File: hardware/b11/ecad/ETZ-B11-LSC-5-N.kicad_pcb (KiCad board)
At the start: 2 copper layers, 112.3 x 85.8 mm, 36 parts, among them SW1 MX-Hotswap-1U, SW10 MX-Hotswap-1U, SW11 MX-Hotswap-1U, SW12 MX-Hotswap-1U, SW13 MX-Hotswap-1U, SW14 MX-Hotswap-1U, SW15 MX-Hotswap-1U, SW16 MX-Hotswap-1U, SW17 MX-Hotswap-1U, SW18 MX-Hotswap-1U, SW2 MX-Hotswap-1U, SW3 MX-Hotswap-1U, SW4 MX-Hotswap-1U, SW5 MX-Hotswap-1U, SW6 MX-Hotswap-1U, SW7 MX-Hotswap-1U, SW8 MX-Hotswap-1U, SW9 MX-Hotswap-1U

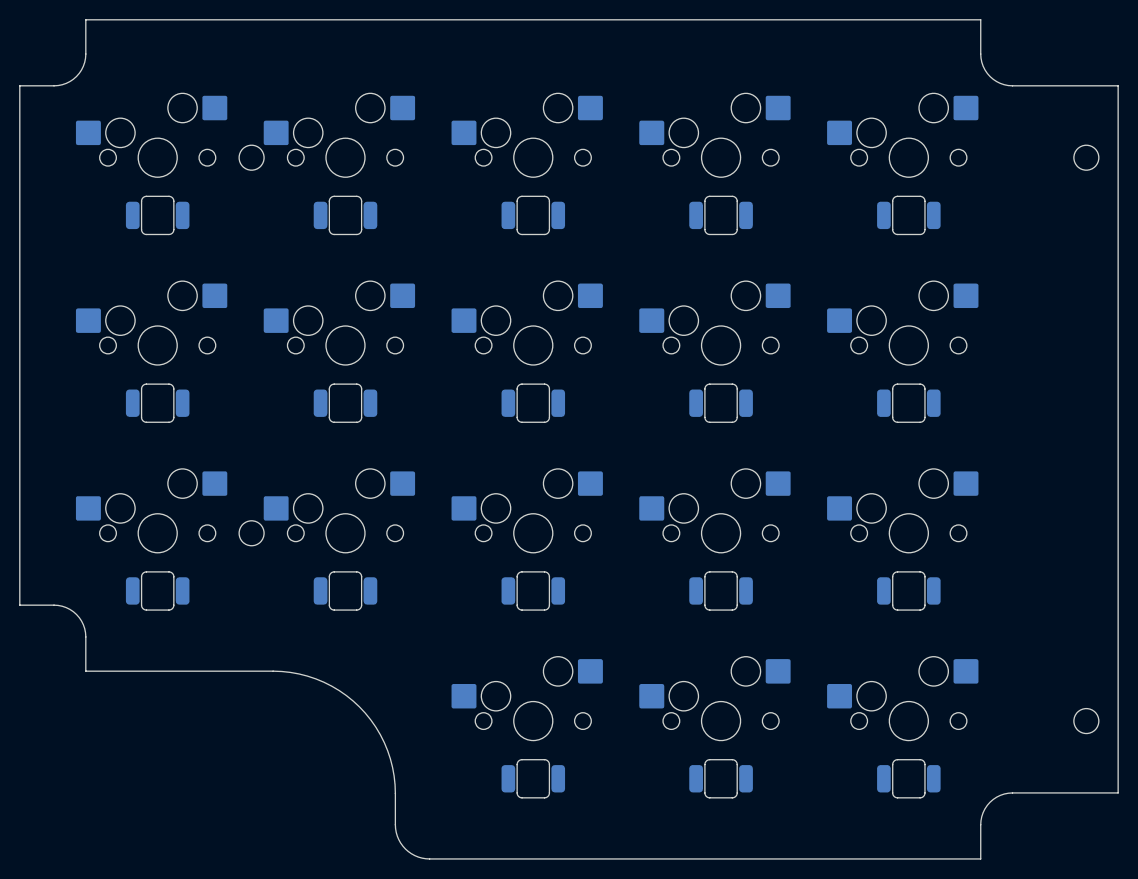
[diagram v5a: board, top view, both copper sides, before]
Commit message: fix(hardware/b11): adjust LED offset to 5.0mm and regenerate all carrier PCBs
Reduces south-facing LED offset from 5.9mm to 5.0mm (closer to the
standard 5.08mm switch-to-LED spacing). All 8 carrier PCBs regenerated.

Co-Authored-By: Claude Sonnet 4.6 <noreply@anthropic.com>
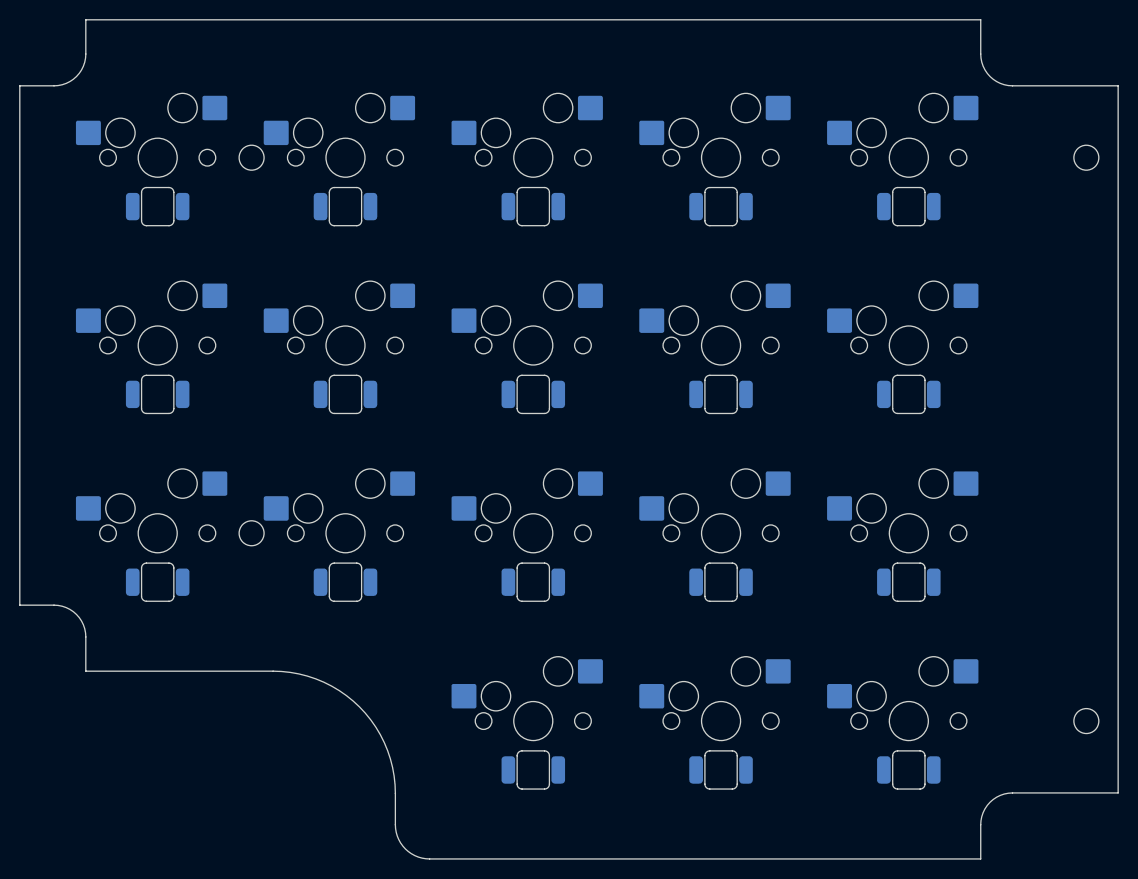
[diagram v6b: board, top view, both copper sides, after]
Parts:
- moved LED11 0.90 mm to (106.4, 116.7)
- moved LED12 0.90 mm to (125.6, 116.7)
- moved LED13 0.90 mm to (144.8, 116.7)
- moved LED14 0.90 mm to (164.0, 116.7)
- moved LED15 0.90 mm to (183.2, 116.7)
- moved LED1 0.90 mm to (106.4, 78.3)
- moved LED10 0.90 mm to (183.2, 97.5)
- moved LED16 0.90 mm to (144.8, 135.9)
- moved LED17 0.90 mm to (164.0, 135.9)
- moved LED18 0.90 mm to (183.2, 135.9)
- moved LED2 0.90 mm to (125.6, 78.3)
- moved LED3 0.90 mm to (144.8, 78.3)
- moved LED4 0.90 mm to (164.0, 78.3)
- moved LED5 0.90 mm to (183.2, 78.3)
- moved LED6 0.90 mm to (106.4, 97.5)
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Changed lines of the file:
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@@
 	(footprint "LED_SMD_6028_BackMount"
 		(layer "B.Cu")
-		(at 164.049999 136.799999)
+		(at 164.049999 78.3)
 		(descr "SMD 6028 back-paste reverse-mount LED, 5.88x2.80mm body, 3.20mm lens, slot 3.3x6.2mm")
 		(tags "LED SMD 6028 reverse-mount back-paste backlighting Choc")
-		(property "Reference" "LED17"
+		(property "Reference" "LED4"
 			(at 0 -2 0)
 			(layer "B.Fab")
@@
 	(footprint "LED_SMD_6028_BackMount"
 		(layer "B.Cu")
-		(at 106.449999 79.2)
+		(at 183.249999 78.3)
 		(descr "SMD 6028 back-paste reverse-mount LED, 5.88x2.80mm body, 3.20mm lens, slot 3.3x6.2mm")
 		(tags "LED SMD 6028 reverse-mount back-paste backlighting Choc")
-		(property "Reference" "LED1"
+		(property "Reference" "LED5"
 			(at 0 -2 0)
 			(layer "B.Fab")
@@
 	(footprint "LED_SMD_6028_BackMount"
 		(layer "B.Cu")
-		(at 183.249999 117.6)
+		(at 164.049999 135.899999)
 		(descr "SMD 6028 back-paste reverse-mount LED, 5.88x2.80mm body, 3.20mm lens, slot 3.3x6.2mm")
 		(tags "LED SMD 6028 reverse-mount back-paste backlighting Choc")
-		(property "Reference" "LED15"
+		(property "Reference" "LED17"
 			(at 0 -2 0)
 			(layer "B.Fab")
@@
 	(footprint "LED_SMD_6028_BackMount"
 		(layer "B.Cu")
-		(at 106.449999 117.6)
+		(at 183.249999 97.5)
 		(descr "SMD 6028 back-paste reverse-mount LED, 5.88x2.80mm body, 3.20mm lens, slot 3.3x6.2mm")
 		(tags "LED SMD 6028 reverse-mount back-paste backlighting Choc")
-		(property "Reference" "LED11"
+		(property "Reference" "LED10"
 			(at 0 -2 0)
 			(layer "B.Fab")
@@
 	(footprint "LED_SMD_6028_BackMount"
 		(layer "B.Cu")
-		(at 183.249999 98.4)
+		(at 125.649999 97.5)
 		(descr "SMD 6028 back-paste reverse-mount LED, 5.88x2.80mm body, 3.20mm lens, slot 3.3x6.2mm")
 		(tags "LED SMD 6028 reverse-mount back-paste backlighting Choc")
-		(property "Reference" "LED10"
+		(property "Reference" "LED7"
 			(at 0 -2 0)
 			(layer "B.Fab")
@@
 	(footprint "LED_SMD_6028_BackMount"
 		(layer "B.Cu")
-		(at 125.649999 117.6)
+		(at 144.849999 135.899999)
 		(descr "SMD 6028 back-paste reverse-mount LED, 5.88x2.80mm body, 3.20mm lens, slot 3.3x6.2mm")
 		(tags "LED SMD 6028 reverse-mount back-paste backlighting Choc")
-		(property "Reference" "LED12"
+		(property "Reference" "LED16"
 			(at 0 -2 0)
 			(layer "B.Fab")
@@
 	(footprint "LED_SMD_6028_BackMount"
 		(layer "B.Cu")
-		(at 183.249999 79.2)
+		(at 106.449999 97.5)
 		(descr "SMD 6028 back-paste reverse-mount LED, 5.88x2.80mm body, 3.20mm lens, slot 3.3x6.2mm")
 		(tags "LED SMD 6028 reverse-mount back-paste backlighting Choc")
-		(property "Reference" "LED5"
+		(property "Reference" "LED6"
 			(at 0 -2 0)
 			(layer "B.Fab")
@@
 	(footprint "LED_SMD_6028_BackMount"
 		(layer "B.Cu")
-		(at 144.849999 117.6)
+		(at 106.449999 116.699999)
 		(descr "SMD 6028 back-paste reverse-mount LED, 5.88x2.80mm body, 3.20mm lens, slot 3.3x6.2mm")
 		(tags "LED SMD 6028 reverse-mount back-paste backlighting Choc")
-		(property "Reference" "LED13"
+		(property "Reference" "LED11"
 			(at 0 -2 0)
 			(layer "B.Fab")
@@
 	(footprint "LED_SMD_6028_BackMount"
 		(layer "B.Cu")
-		(at 164.049999 98.4)
+		(at 106.449999 78.3)
 		(descr "SMD 6028 back-paste reverse-mount LED, 5.88x2.80mm body, 3.20mm lens, slot 3.3x6.2mm")
 		(tags "LED SMD 6028 reverse-mount back-paste backlighting Choc")
-		(property "Reference" "LED9"
+		(property "Reference" "LED1"
 			(at 0 -2 0)
 			(layer "B.Fab")
@@
 	(footprint "LED_SMD_6028_BackMount"
 		(layer "B.Cu")
-		(at 144.849999 79.2)
+		(at 125.649999 116.699999)
 		(descr "SMD 6028 back-paste reverse-mount LED, 5.88x2.80mm body, 3.20mm lens, slot 3.3x6.2mm")
 		(tags "LED SMD 6028 reverse-mount back-paste backlighting Choc")
-		(property "Reference" "LED3"
+		(property "Reference" "LED12"
 			(at 0 -2 0)
 			(layer "B.Fab")
@@
 	(footprint "LED_SMD_6028_BackMount"
 		(layer "B.Cu")
-		(at 125.649999 98.4)
+		(at 144.849999 116.699999)
 		(descr "SMD 6028 back-paste reverse-mount LED, 5.88x2.80mm body, 3.20mm lens, slot 3.3x6.2mm")
 		(tags "LED SMD 6028 reverse-mount back-paste backlighting Choc")
-		(property "Reference" "LED7"
+		(property "Reference" "LED13"
 			(at 0 -2 0)
 			(layer "B.Fab")
@@
 	(footprint "LED_SMD_6028_BackMount"
 		(layer "B.Cu")
-		(at 164.049999 117.6)
+		(at 183.249999 116.699999)
 		(descr "SMD 6028 back-paste reverse-mount LED, 5.88x2.80mm body, 3.20mm lens, slot 3.3x6.2mm")
 		(tags "LED SMD 6028 reverse-mount back-paste backlighting Choc")
-		(property "Reference" "LED14"
+		(property "Reference" "LED15"
 			(at 0 -2 0)
 			(layer "B.Fab")
@@
 	(footprint "LED_SMD_6028_BackMount"
 		(layer "B.Cu")
-		(at 125.649999 79.2)
+		(at 164.049999 116.699999)
 		(descr "SMD 6028 back-paste reverse-mount LED, 5.88x2.80mm body, 3.20mm lens, slot 3.3x6.2mm")
 		(tags "LED SMD 6028 reverse-mount back-paste backlighting Choc")
-		(property "Reference" "LED2"
+		(property "Reference" "LED14"
 			(at 0 -2 0)
 			(layer "B.Fab")
@@
 	(footprint "LED_SMD_6028_BackMount"
 		(layer "B.Cu")
-		(at 183.249999 136.799999)
+		(at 164.049999 97.5)
 		(descr "SMD 6028 back-paste reverse-mount LED, 5.88x2.80mm body, 3.20mm lens, slot 3.3x6.2mm")
 		(tags "LED SMD 6028 reverse-mount back-paste backlighting Choc")
-		(property "Reference" "LED18"
+		(property "Reference" "LED9"
 			(at 0 -2 0)
 			(layer "B.Fab")
@@
 	(footprint "LED_SMD_6028_BackMount"
 		(layer "B.Cu")
-		(at 106.449999 98.4)
+		(at 144.849999 78.3)
 		(descr "SMD 6028 back-paste reverse-mount LED, 5.88x2.80mm body, 3.20mm lens, slot 3.3x6.2mm")
 		(tags "LED SMD 6028 reverse-mount back-paste backlighting Choc")
-		(property "Reference" "LED6"
+		(property "Reference" "LED3"
 			(at 0 -2 0)
 			(layer "B.Fab")
@@
 	(footprint "LED_SMD_6028_BackMount"
 		(layer "B.Cu")
-		(at 164.049999 79.2)
+		(at 125.649999 78.3)
 		(descr "SMD 6028 back-paste reverse-mount LED, 5.88x2.80mm body, 3.20mm lens, slot 3.3x6.2mm")
 		(tags "LED SMD 6028 reverse-mount back-paste backlighting Choc")
-		(property "Reference" "LED4"
+		(property "Reference" "LED2"
 			(at 0 -2 0)
 			(layer "B.Fab")
@@
 	(footprint "LED_SMD_6028_BackMount"
 		(layer "B.Cu")
-		(at 144.849999 98.4)
+		(at 183.249999 135.899999)
 		(descr "SMD 6028 back-paste reverse-mount LED, 5.88x2.80mm body, 3.20mm lens, slot 3.3x6.2mm")
 		(tags "LED SMD 6028 reverse-mount back-paste backlighting Choc")
-		(property "Reference" "LED8"
+		(property "Reference" "LED18"
 			(at 0 -2 0)
 			(layer "B.Fab")
@@
 	(footprint "LED_SMD_6028_BackMount"
 		(layer "B.Cu")
-		(at 144.849999 136.799999)
+		(at 144.849999 97.5)
 		(descr "SMD 6028 back-paste reverse-mount LED, 5.88x2.80mm body, 3.20mm lens, slot 3.3x6.2mm")
 		(tags "LED SMD 6028 reverse-mount back-paste backlighting Choc")
-		(property "Reference" "LED16"
+		(property "Reference" "LED8"
 			(at 0 -2 0)
 			(layer "B.Fab")
